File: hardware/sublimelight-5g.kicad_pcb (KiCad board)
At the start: 2 copper layers, 22 parts, among them J3 Barrel_Jack_Switch, J4 Conn_01x05, J5 Barrel_Jack_Switch, SW1 SW_Push, U1 ST1480ACDR, U2 ESP32-WROOM-32D, U3 LDD-H, U4 LDD-H, U5 VXO7803-1000

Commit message: first placement
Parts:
- added H1: MountingHole, MountingHole:MountingHole_3.2mm_M3, F.Cu at (75.0, 55.0)
- added H2: MountingHole, MountingHole:MountingHole_3.2mm_M3, F.Cu at (75.0, 130.0)
- added H3: MountingHole, MountingHole:MountingHole_3.2mm_M3, F.Cu at (122.0, 55.0)
- added H4: MountingHole, MountingHole:MountingHole_3.2mm_M3, F.Cu at (145.0, 130.0)
- added J1: RJ45, MTJ-88TX1-FSD-PGB:RJ45_MTJ-88TX1-FSD-PGB, F.Cu at (132.7, 84.5)
- added J2: RJ45, MTJ-88TX1-FSD-PGB:RJ45_MTJ-88TX1-FSD-PGB, F.Cu at (132.7, 65.4)
- added J6: Conn_01x02, TBL005A-500:TBL005A-500-02, F.Cu at (90.8, 124.5)
- moved J5 78.7 mm to (136.5, 100.3)
- moved J3 77.4 mm to (136.5, 118.7)
- moved U4 77.2 mm to (117.5, 100.3)
- moved U3 77.0 mm to (117.5, 121.3)
- moved SW1 61.2 mm to (98.4, 54.0)
- moved JP1 61.2 mm to (91.4, 64.1)
- moved R3 57.5 mm to (117.9, 64.5)
- moved JP2 57.5 mm to (121.9, 66.9)
- moved U2 55.5 mm to (85.7, 78.1)
- moved C3 55.2 mm to (78.1, 89.5), turned to 180 degrees
- moved R1 54.7 mm to (81.3, 92.7), turned to 0 degrees
- moved C2 53.8 mm to (113.7, 62.2)
- moved U1 53.8 mm to (111.1, 66.0)
- moved C1 52.8 mm to (81.9, 95.2), turned to -90 degrees
- moved J4 49.0 mm to (92.1, 54.6)
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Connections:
- U1 pad 2: /DE -> /RTS
- U1 pad 3: /DE -> /RTS
- U2 pad 26: (no net) -> /RTS
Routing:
- added copper zone on B.Cu, net GND
- added copper zone on F.Cu, net GND
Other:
- board outline added: 80 x 85 mm

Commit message: change net class parameters
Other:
- net class Default: trace_width 0.25 -> 0.2; via_dia 0.8 -> 0.6; via_drill 0.4 -> 0.3
- rule trace_min: 0.2 -> 0.15
- rule via_min_size: 0.4 -> 0.6
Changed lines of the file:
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@@
   )
   (setup
-    (last_trace_width 0.25)
+    (stackup
+      (layer "F.SilkS" (type "Top Silk Screen"))
+      (layer "F.Paste" (type "Top Solder Paste"))
+      (layer "F.Mask" (type "Top Solder Mask") (thickness 0.01) (color "Green"))
+      (layer "F.Cu" (type "copper") (thickness 0.035))
+      (layer "dielectric 1" (type "core") (thickness 1.51) (material "FR4") (epsilon_r 4.5) (loss_tangent 0.02))
+      (layer "B.Cu" (type "copper") (thickness 0.035))
+      (layer "B.Mask" (type "Bottom Solder Mask") (thickness 0.01) (color "Green"))
+      (layer "B.Paste" (type "Bottom Solder Paste"))
+      (layer "B.SilkS" (type "Bottom Silk Screen"))
+      (copper_finish "None")
+      (dielectric_constraints no)
+    )
+    (last_trace_width 0.2)
     (trace_clearance 0.2)
     (zone_clearance 0.15)
     (zone_45_only no)
-    (trace_min 0.2)
-    (via_size 0.8)
-    (via_drill 0.4)
-    (via_min_size 0.4)
+    (trace_min 0.15)
+    (via_size 0.6)
+    (via_drill 0.3)
+    (via_min_size 0.6)
     (via_min_drill 0.3)
     (uvia_size 0.3)
@@
   (net_class "Default" "This is the default net class."
     (clearance 0.2)
-    (trace_width 0.25)
-    (via_dia 0.8)
-    (via_drill 0.4)
+    (trace_width 0.2)
+    (via_dia 0.6)
+    (via_drill 0.3)
     (uvia_dia 0.3)
     (uvia_drill 0.1)

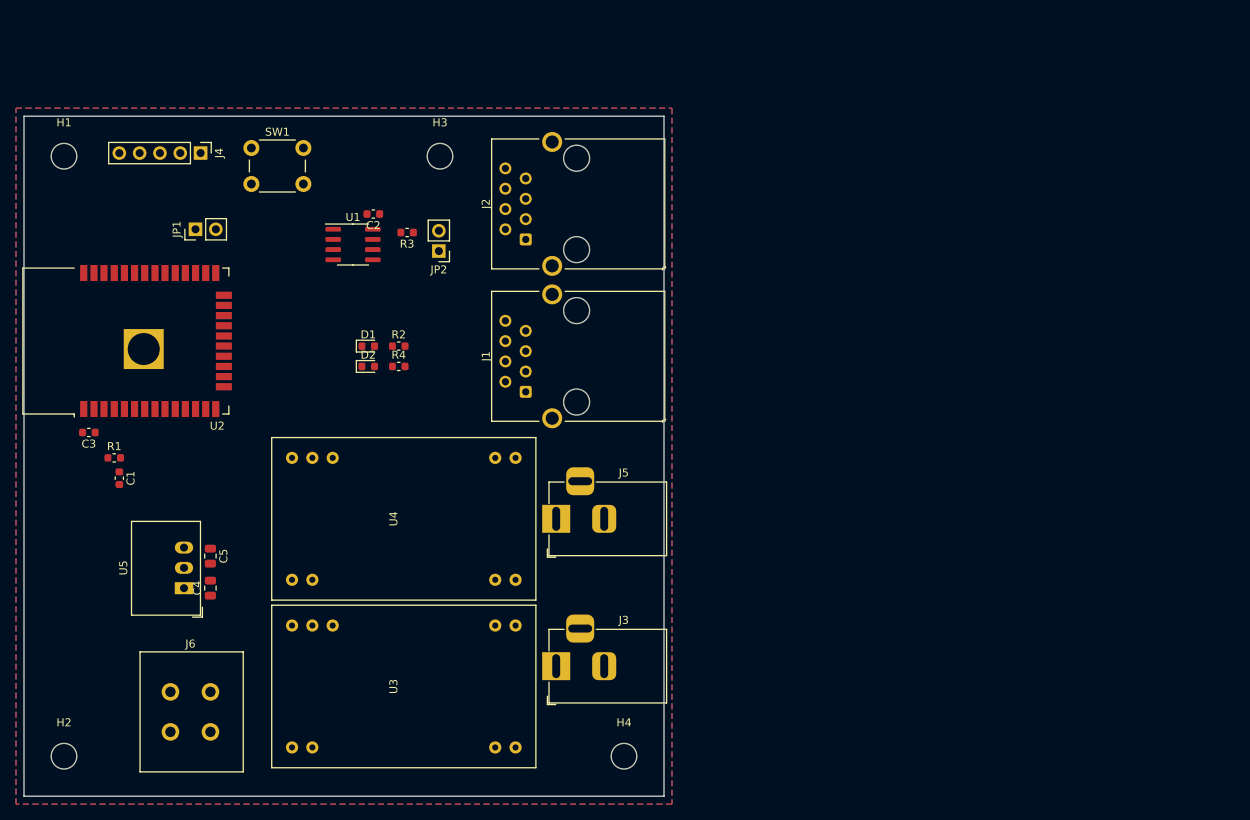
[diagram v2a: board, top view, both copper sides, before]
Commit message: schematics mostly done; layout not finished yet
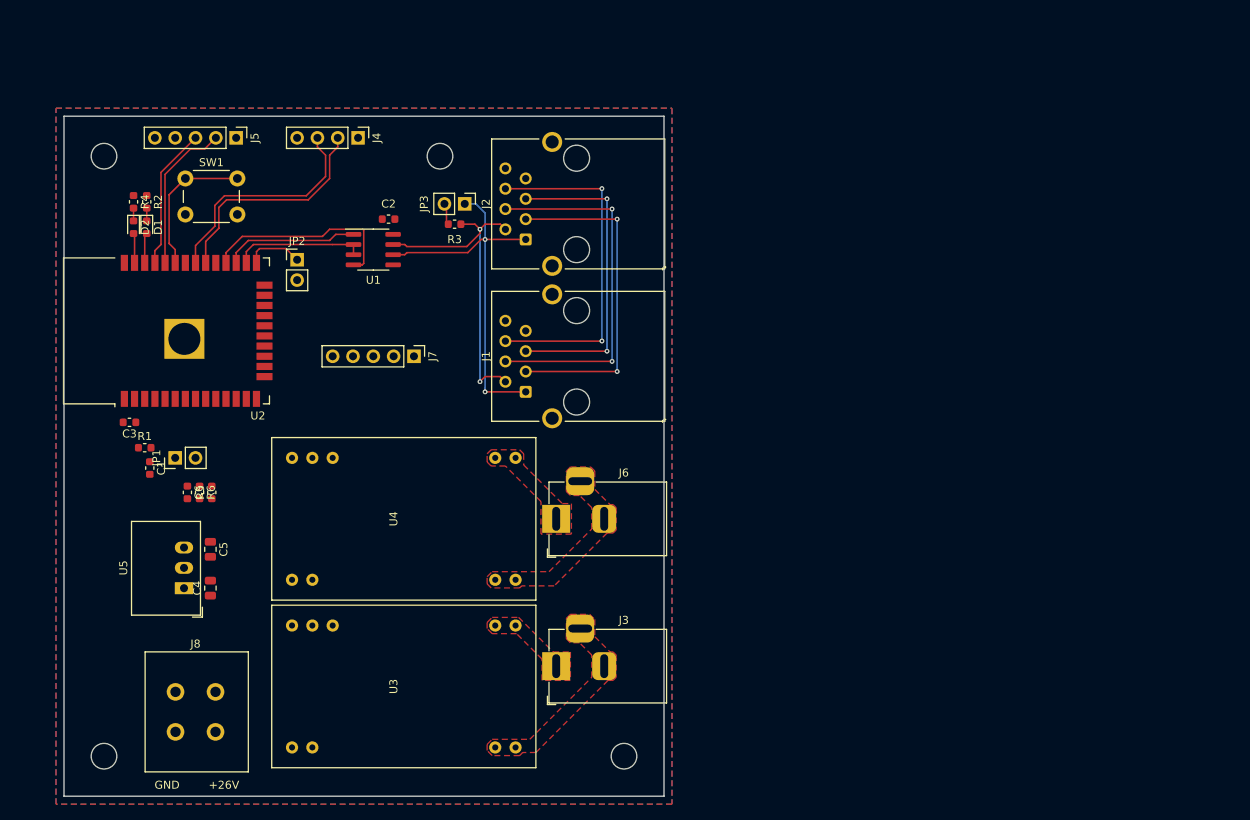
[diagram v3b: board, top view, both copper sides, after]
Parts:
- removed the JP2 at (121.9, 66.9)
- added C6: 100n, Capacitor_SMD:C_0603_1608Metric, F.Cu at (90.4, 97.0)
- added J4: Conn_01x04, Connector_PinHeader_2.54mm:PinHeader_1x04_P2.54mm_Vertical, F.Cu at (111.8, 52.7)
- added J7: Conn_01x05, Connector_PinHeader_2.54mm:PinHeader_1x05_P2.54mm_Vertical, F.Cu at (118.7, 80.0)
- added JP1: Jumper_2_Open, Connector_PinHeader_2.54mm:PinHeader_1x02_P2.54mm_Vertical, F.Cu at (88.9, 92.7)
- added JP3: Jumper_2_Open, Connector_PinHeader_2.54mm:PinHeader_1x02_P2.54mm_Vertical, F.Cu at (125.1, 61.0)
- added R5: 100k, Resistor_SMD:R_0603_1608Metric, F.Cu at (93.5, 97.0)
- added R6: 10k, Resistor_SMD:R_0603_1608Metric, F.Cu at (91.9, 97.0)
- moved R4 39.0 mm to (83.7, 60.7), turned to -90 degrees
- moved R2 36.3 mm to (85.3, 60.7), turned to -90 degrees
- moved D2 34.1 mm to (83.7, 63.9), turned to -90 degrees
- moved D1 31.4 mm to (85.3, 63.9), turned to -90 degrees
- moved JP2 13.3 mm to (104.1, 67.9), turned to 0 degrees
- moved SW1 9.09 mm to (90.2, 57.8)
- moved R3 6.03 mm to (123.8, 63.5), turned to 0 degrees
- moved U2 5.24 mm to (90.8, 76.8)
- moved C3 5.24 mm to (83.2, 88.3)
- moved H1 5.00 mm to (80.0, 55.0)
- moved H2 5.00 mm to (80.0, 130.0)
- moved J5 4.84 mm to (96.5, 52.7)
- moved R1 4.02 mm to (85.1, 91.4)
- moved C1 4.02 mm to (85.7, 94.0)
- moved U1 2.62 mm to (113.7, 66.7)
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- renumbered J4 to J5, J5 to J6, J6 to J8, JP1 to JP2
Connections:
- D1 pad 1: GND -> Net-(D1-Pad1)
- D1 pad 2: Net-(D1-Pad2) -> /LED0
- D2 pad 1: GND -> Net-(D2-Pad1)
- D2 pad 2: Net-(D2-Pad2) -> /LED1
- J1 pad SH: Net-(J1-PadSH) -> GND
- J2 pad SH: Net-(J2-PadSH) -> GND
- R2 pad 1: Net-(D1-Pad2) -> GND
- R2 pad 2: (no net) -> Net-(D1-Pad1)
- R4 pad 1: Net-(D2-Pad2) -> GND
- R4 pad 2: (no net) -> Net-(D2-Pad1)
- U2 pad 10: (no net) -> /AUX_1_0
- U2 pad 11: (no net) -> /AUX_1_1
- U2 pad 12: (no net) -> /AUX_1_2
- U2 pad 30: (no net) -> /AUX_0_0
- U2 pad 31: (no net) -> /AUX_0_1
- U2 pad 33: (no net) -> /TASTER
- U2 pad 36: (no net) -> /LED0
- U2 pad 37: (no net) -> /LED1
- U2 pad 6: (no net) -> /V_SENSE
- U2 pad 8: (no net) -> /PWM_W_COLD
- U2 pad 9: (no net) -> /PWM_W_WARM
- U3 pad 22: (no net) -> /PWM_W_COLD
- U4 pad 22: (no net) -> /PWM_W_WARM
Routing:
- net /RS485_A: track 0.00 -> 48.6 mm, vias 0 -> 2
- net /RJ45_4: track 0.00 -> 45.7 mm, vias 0 -> 2
- net /RJ45_6: track 0.00 -> 43.2 mm, vias 0 -> 2
- net /RJ45_3: track 0.00 -> 41.9 mm, vias 0 -> 2
- net /RS485_B: track 0.00 -> 41.3 mm, vias 0 -> 2
- net /RJ45_5: track 0.00 -> 39.4 mm, vias 0 -> 2
- net /AUX_0_1: track 0.00 -> 28.8 mm
- net /AUX_0_0: track 0.00 -> 28.5 mm
- net /DI: track 0.00 -> 25.3 mm
- net /USB_TXD: track 0.00 -> 19.3 mm
- net /TASTER: track 0.00 -> 18.2 mm
- net /USB_RXD: track 0.00 -> 17.7 mm
- net /RO: track 0.00 -> 16.9 mm
- net /RTS: track 0.00 -> 16.4 mm
- net /IO0: track 0.00 -> 7.61 mm
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- added copper zone on F.Cu, net /W_COLD+
- added copper zone on F.Cu, net /W_COLD-
- added copper zone on F.Cu, net /W_WARM+
- added copper zone on F.Cu, net /W_WARM-
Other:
- board size 80 x 85 mm -> 75 x 85 mm
- board text added: "+26V"
- board text added: "GND"

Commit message: route board
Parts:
- moved JP3 11.9 mm to (121.9, 72.4), turned to 180 degrees
- moved R3 8.35 mm to (125.1, 71.8), turned to -90 degrees
- moved R5 5.29 mm to (97.8, 94.0)
- moved R6 5.29 mm to (96.3, 94.0)
- moved C6 5.29 mm to (94.7, 94.0)
- moved C1 4.58 mm to (88.3, 90.2), turned to 0 degrees
- moved J7 3.70 mm to (116.8, 83.2)
- moved C4 3.53 mm to (95.2, 106.0)
- moved U5 3.04 mm to (91.8, 106.6)
- moved C5 2.91 mm to (95.2, 102.0)
- moved JP1 1.42 mm to (87.6, 93.3)
- moved R1 1.27 mm to (85.1, 90.2)
- moved C2 1.02 mm to (116.6, 62.9), turned to 0 degrees
- moved J8 0.64 mm to (91.4, 125.1)
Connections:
- JP3 pad 1: /RS485_A -> Net-(JP3-Pad1)
- JP3 pad 2: Net-(JP3-Pad2) -> /RS485_B
- R3 pad 1: Net-(JP3-Pad2) -> /RS485_A
- R3 pad 2: /RS485_B -> Net-(JP3-Pad1)
- U2 pad 8: /PWM_W_COLD -> /PWM_W_WARM
- U2 pad 9: /PWM_W_WARM -> /PWM_W_COLD
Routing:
- net +3V3: track 0.00 -> 99.2 mm, vias 0 -> 4
- net /PWM_W_COLD: track 0.00 -> 46.8 mm
- net /AUX_1_0: track 0.00 -> 24.6 mm
- net /PWM_W_WARM: track 0.00 -> 22.1 mm
- net /AUX_1_1: track 0.00 -> 21.5 mm
- net /AUX_1_2: track 0.00 -> 18.2 mm
- net /V_SENSE: track 0.00 -> 13.9 mm
- net +28V: track 0.00 -> 12.4 mm
- net /EN: track 0.00 -> 10.00 mm
- net /RS485_B: track 41.3 -> 46.2 mm, vias 2 -> 1
- net Net-(JP3-Pad1): track 0.00 -> 3.24 mm
- net /RJ45_4: track 45.7 -> 42.7 mm
- net /RJ45_3: track 41.9 -> 39.0 mm
- net Net-(JP3-Pad2): track 2.74 -> 0.00 mm
- net /RJ45_5: track 39.4 -> 36.7 mm
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- added copper zone on F.Cu, net +28V
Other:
- net class power added: clearance 0.2, trace_width 0.3, via_dia 0.6, via_drill 0.3

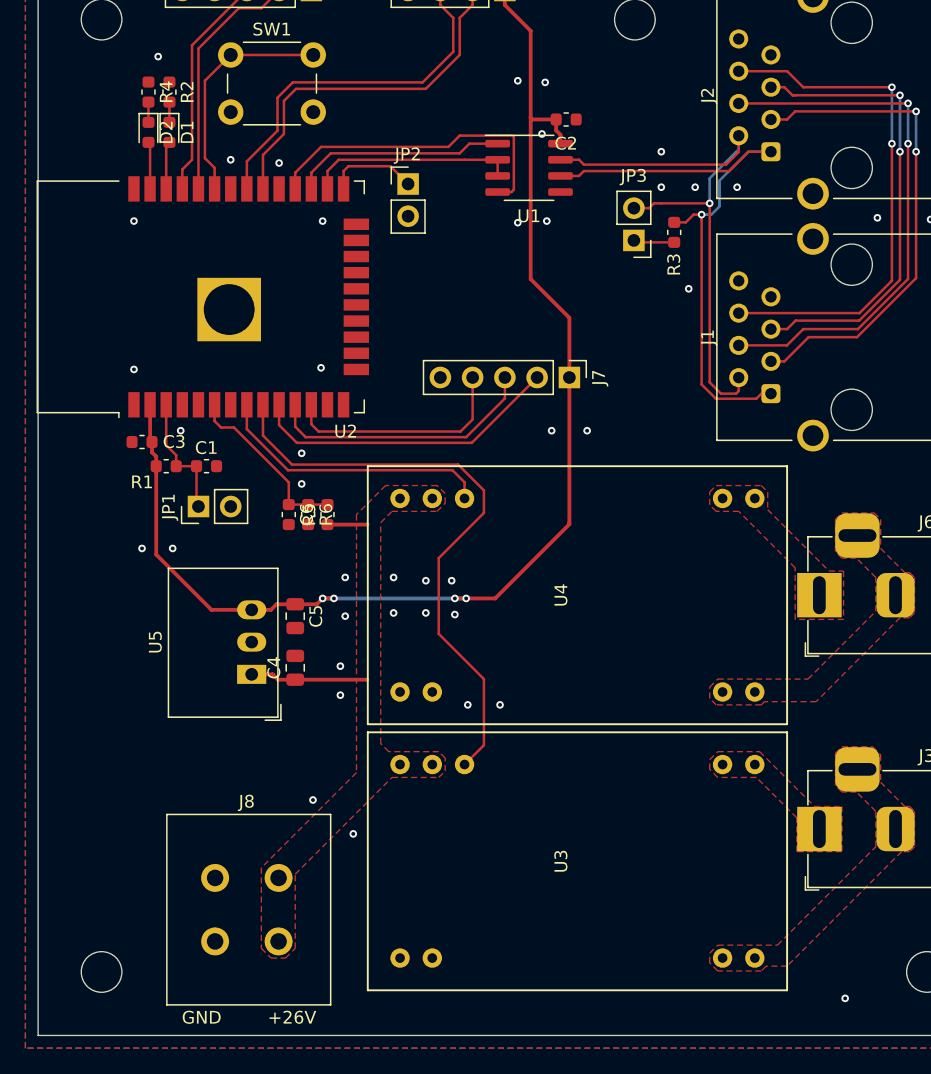
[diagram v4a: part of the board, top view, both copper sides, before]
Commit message: add logo to board and clean up silkscreen
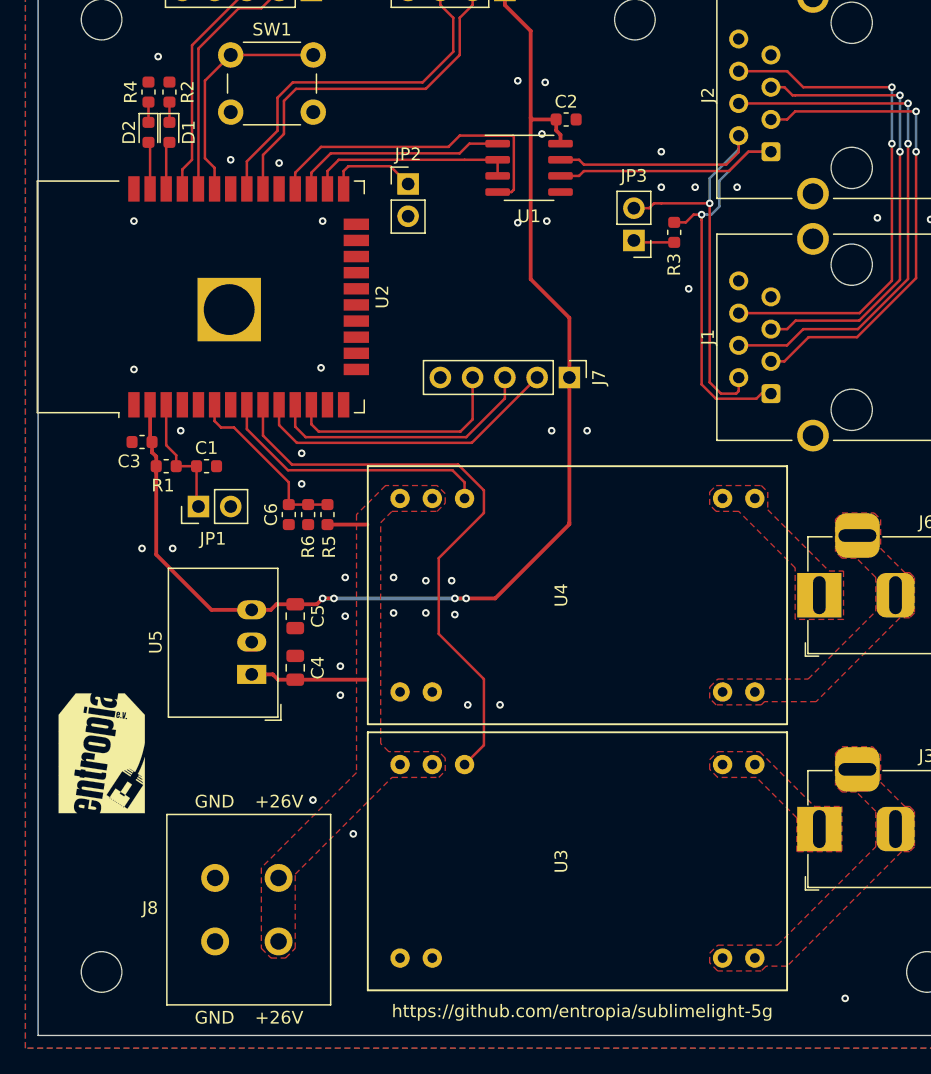
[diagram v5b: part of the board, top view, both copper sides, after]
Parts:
- added G***: LOGO, logos:entropia, F.Cu at (80.0, 112.8)
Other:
- board text added: "https://github.com/entropia/sublimelight-5g"
